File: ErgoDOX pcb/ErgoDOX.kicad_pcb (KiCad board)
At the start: 2 copper layers, 182.8 x 158.9 mm, 77 parts, among them J1 USB, J2 3.5mm, J3 JMP, J4 JMP, SW0:10 SW0:3, SW0:11 SW0:2, SW0:12 SW0:1, SW0:7 SW0:6, SW0:8 SW0:5, SW0:9 SW0:4, SW1:10 SW1:3, SW1:11 SW1:2, SW1:12 SW1:1, SW1:13 SW1:0, SW1:9 SW1:4, SW2:10 SW2:3, SW2:11 SW2:2, SW2:12 SW2:1, SW2:13 SW2:0, SW2:7 SW2:6, SW2:8 SW2:5, SW2:9 SW2:4, SW3:10 SW3:3, SW3:11 SW3:2, SW3:12 SW3:1, SW3:13 SW3:0, SW3:8 SW3:5, SW3:9 SW3:4, SW4:10 SW4:3, SW4:11 SW4:2, SW4:12 SW4:1, SW4:13 SW4:0, SW4:7 SW4:6, SW4:8 SW4:5, SW4:9 SW4:4, SW5:10 SW5:3, SW5:11 SW5:2, SW5:12 SW5:1, SW5:13 SW5:0, SW5:7 SW5:6, SW5:8 SW5:5, SW5:9 SW5:4, U1 TEENSY2.0, U2 MCP23018

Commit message: //WIP
Switches replaced
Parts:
- removed STAR_1: STAR_FRONT, ErgoDOX pcb:STAR
- removed STAR_2: STAR_BACK, ErgoDOX pcb:STAR
- removed STITCHING_VIA (x11): ~, lib_footprints:STITCHING_VIA
- added D1: DIODE, Diode_THT:D_DO-35_SOD27_P7.62mm_Horizontal, F.Cu at (68.6, 73.7)
- added D10: DIODE, Diode_THT:D_DO-35_SOD27_P7.62mm_Horizontal, F.Cu at (87.6, 111.8)
- added D11: DIODE, Diode_THT:D_DO-35_SOD27_P7.62mm_Horizontal, F.Cu at (106.7, 91.4)
- added D12: DIODE, Diode_THT:D_DO-35_SOD27_P7.62mm_Horizontal, F.Cu at (106.7, 110.5)
- added D13: DIODE, Diode_THT:D_DO-35_SOD27_P7.62mm_Horizontal, F.Cu at (125.7, 90.2)
- added D15: DIODE, Diode_THT:D_DO-35_SOD27_P7.62mm_Horizontal, F.Cu at (152.4, 91.4)
- added D16: DIODE, Diode_THT:D_DO-35_SOD27_P7.62mm_Horizontal, F.Cu at (152.4, 110.5)
- added D17: DIODE, Diode_THT:D_DO-35_SOD27_P7.62mm_Horizontal, F.Cu at (163.8, 95.2)
- added D18: DIODE, Diode_THT:D_DO-35_SOD27_P7.62mm_Horizontal, F.Cu at (163.8, 114.3)
- added D19: DIODE, Diode_THT:D_DO-35_SOD27_P7.62mm_Horizontal, F.Cu at (188.0, 95.2)
- added D2: DIODE, Diode_THT:D_DO-35_SOD27_P7.62mm_Horizontal, F.Cu at (87.6, 73.7)
- added D20: DIODE, Diode_THT:D_DO-35_SOD27_P7.62mm_Horizontal, F.Cu at (188.0, 114.3)
- added D21: DIODE, Diode_THT:D_DO-35_SOD27_P7.62mm_Horizontal, F.Cu at (81.3, 120.7)
- added D22: DIODE, Diode_THT:D_DO-35_SOD27_P7.62mm_Horizontal, F.Cu at (87.6, 130.8)
- added D23: DIODE, Diode_THT:D_DO-35_SOD27_P7.62mm_Horizontal, F.Cu at (106.7, 129.5)
- added D24: DIODE, Diode_THT:D_DO-35_SOD27_P7.62mm_Horizontal, F.Cu at (125.7, 128.3)
- added D25: DIODE, Diode_THT:D_DO-35_SOD27_P7.62mm_Horizontal, F.Cu at (152.4, 129.5)
- added D26: DIODE, Diode_THT:D_DO-35_SOD27_P7.62mm_Horizontal, F.Cu at (163.8, 133.3)
- added D27: DIODE, Diode_THT:D_DO-35_SOD27_P7.62mm_Horizontal, F.Cu at (188.0, 133.3)
- added D3: DIODE, Diode_THT:D_DO-35_SOD27_P7.62mm_Horizontal, F.Cu at (106.7, 72.4)
- added D4: DIODE, Diode_THT:D_DO-35_SOD27_P7.62mm_Horizontal, F.Cu at (125.7, 71.1)
- added D5: DIODE, Diode_THT:D_DO-35_SOD27_P7.62mm_Horizontal, F.Cu at (144.8, 72.4)
- added D6: DIODE, Diode_THT:D_DO-35_SOD27_P7.62mm_Horizontal, F.Cu at (163.8, 76.2)
- added D7: DIODE, Diode_THT:D_DO-35_SOD27_P7.62mm_Horizontal, F.Cu at (188.0, 76.2)
- added D8: DIODE, Diode_THT:D_DO-35_SOD27_P7.62mm_Horizontal, F.Cu at (81.3, 92.7)
- added D9: DIODE, Diode_THT:D_DO-35_SOD27_P7.62mm_Horizontal, F.Cu at (87.6, 92.7)
- SW0:10, SW0:11, SW0:12, SW0:7, SW0:8, SW0:9, SW1:10, SW1:11, SW1:12, SW1:13, SW1:9, SW2:10, SW2:11, SW2:12, SW2:7, SW2:8, SW2:9, SW3:10, SW3:11, SW3:12, SW3:8, SW3:9, SW4:10, SW4:11, SW4:12, SW4:7, SW4:8, SW4:9, SW5:10, SW5:11, SW5:12, SW5:7, SW5:8, SW5:9: footprint ErgoDOX pcb:MX_FLIP_DIODE -> Keyswitches Pretty:SW_PG1350_reversible
- SW2:13, SW3:13, SW4:13, SW5:13: footprint ErgoDOX pcb:MX_FLIP_XX -> Keyswitches Pretty:SW_PG1350_reversible
- SX0:10, SX0:11, SX1:7, SX1:8: footprint MX_FLIP -> Keyswitches Pretty:SW_PG1350_reversible
- moved LED_B1 10.2 mm to (62.2, 88.9)
- moved LED_C1 10.2 mm to (62.2, 117.5)
- moved LED_A1 9.22 mm to (72.4, 55.9)
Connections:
- SW0:10 pad 2: Net-(SW0:10-Pad2) -> Net-(D1:4-Pad1)
- SW0:11 pad 2: Net-(SW0:11-Pad2) -> Net-(D1:5-Pad1)
- SW0:12 pad 2: Net-(SW0:12-Pad2) -> Net-(D1:6-Pad1)
- SW0:7 pad 2: Net-(SW0:7-Pad2) -> Net-(D1:1-Pad1)
- SW0:8 pad 2: Net-(SW0:8-Pad2) -> Net-(D1:2-Pad1)
- SW0:9 pad 2: Net-(SW0:9-Pad2) -> Net-(D1:3-Pad1)
- SW2:10 pad 2: Net-(SW2:10-Pad2) -> Net-(D24-Pad1)
- SW2:11 pad 2: Net-(SW2:11-Pad2) -> Net-(D25-Pad1)
- SW2:12 pad 2: Net-(SW2:12-Pad2) -> Net-(D26-Pad1)
- SW2:13 pad 2: Net-(SW2:13-Pad2) -> Net-(D27-Pad1)
- SW2:7 pad 2: Net-(SW2:7-Pad2) -> Net-(D21-Pad1)
- SW2:8 pad 2: Net-(SW2:8-Pad2) -> Net-(D22-Pad1)
- SW2:9 pad 2: Net-(SW2:9-Pad2) -> Net-(D23-Pad1)
- SW3:10 pad 2: Net-(SW3:10-Pad2) -> Net-(D14-Pad1)
- SW3:11 pad 2: Net-(SW3:11-Pad2) -> Net-(D16-Pad1)
- SW3:12 pad 2: Net-(SW3:12-Pad2) -> Net-(D18-Pad1)
- SW3:13 pad 2: Net-(SW3:13-Pad2) -> Net-(D20-Pad1)
- SW3:8 pad 2: Net-(SW3:8-Pad2) -> Net-(D10-Pad1)
- SW3:9 pad 2: Net-(SW3:9-Pad2) -> Net-(D12-Pad1)
- SW4:10 pad 2: Net-(SW4:10-Pad2) -> Net-(D13-Pad1)
- SW4:11 pad 2: Net-(SW4:11-Pad2) -> Net-(D15-Pad1)
- SW4:12 pad 2: Net-(SW4:12-Pad2) -> Net-(D17-Pad1)
- SW4:13 pad 2: Net-(SW4:13-Pad2) -> Net-(D19-Pad1)
- SW4:7 pad 2: Net-(SW4:7-Pad2) -> Net-(D8-Pad1)
- SW4:8 pad 2: Net-(SW4:8-Pad2) -> Net-(D9-Pad1)
- SW4:9 pad 2: Net-(SW4:9-Pad2) -> Net-(D11-Pad1)
- SW5:10 pad 2: Net-(SW5:10-Pad2) -> Net-(D4-Pad1)
- SW5:11 pad 2: Net-(SW5:11-Pad2) -> Net-(D5-Pad1)
- SW5:12 pad 2: Net-(SW5:12-Pad2) -> Net-(D6-Pad1)
- SW5:13 pad 2: Net-(SW5:13-Pad2) -> Net-(D7-Pad1)
- SW5:7 pad 2: Net-(SW5:7-Pad2) -> Net-(D1-Pad1)
- SW5:8 pad 2: Net-(SW5:8-Pad2) -> Net-(D2-Pad1)
- SW5:9 pad 2: Net-(SW5:9-Pad2) -> Net-(D3-Pad1)
- SX0:10 pad 2: Net-(SW0:10-Pad2) -> Net-(D1:4-Pad1)
- SX0:11 pad 2: Net-(SW0:11-Pad2) -> Net-(D1:5-Pad1)
- U1 pad 12: Net-(U1-Pad12) -> (no net)
- U1 pad 19: Net-(U1-Pad19) -> (no net)
- U2 pad 14: Net-(U2-Pad14) -> (no net)
- U2 pad 17: Net-(U2-Pad17) -> (no net)
- U2 pad 18: Net-(U2-Pad18) -> (no net)
- U2 pad 19: Net-(U2-Pad19) -> (no net)
- U2 pad 27: Net-(U2-Pad27) -> (no net)
- U2 pad 28: Net-(U2-Pad28) -> (no net)
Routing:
- net /COL11: track 316.5 -> 256.5 mm
- net Net-(D20-Pad1): track 0.00 -> 45.5 mm
- net Net-(D19-Pad1): track 0.00 -> 45.4 mm
- net Net-(D7-Pad1): track 0.00 -> 45.4 mm
- net Net-(D27-Pad1): track 0.00 -> 45.0 mm
- net /ROW4: track 257.4 -> 215.6 mm
- net Net-(SW3:13-Pad2): track 38.1 -> 0.00 mm
- net Net-(SW4:13-Pad2): track 38.1 -> 0.00 mm
- net Net-(SW5:13-Pad2): track 38.0 -> 0.00 mm
- net Net-(SW2:13-Pad2): track 37.7 -> 0.00 mm
- net Net-(D1:4-Pad1): track 0.00 -> 29.2 mm
- net Net-(SW0:10-Pad2): track 34.8 -> 5.60 mm
- net Net-(D1:5-Pad1): track 0.00 -> 29.2 mm
- net Net-(SW0:11-Pad2): track 34.8 -> 5.61 mm
- net /COL1: track 291.8 -> 268.0 mm
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
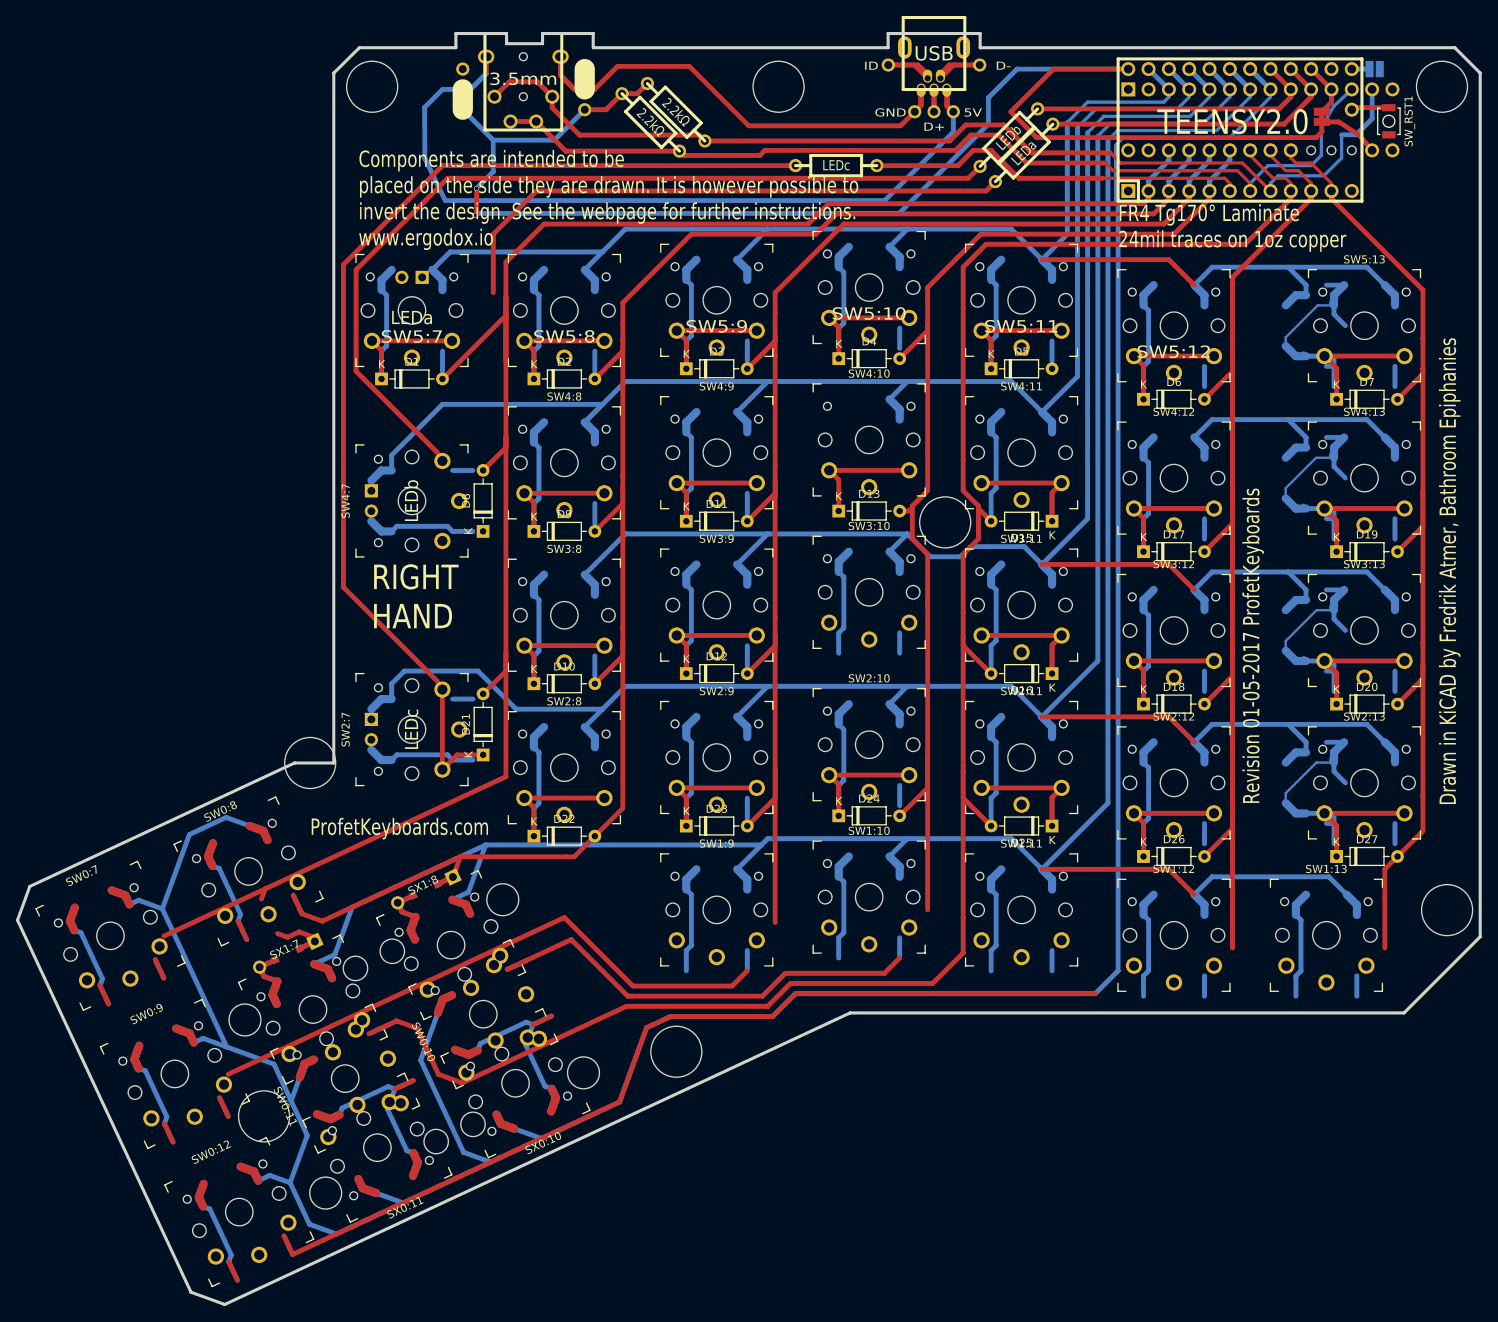
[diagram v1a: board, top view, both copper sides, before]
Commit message: WIP placement.py script, some routing
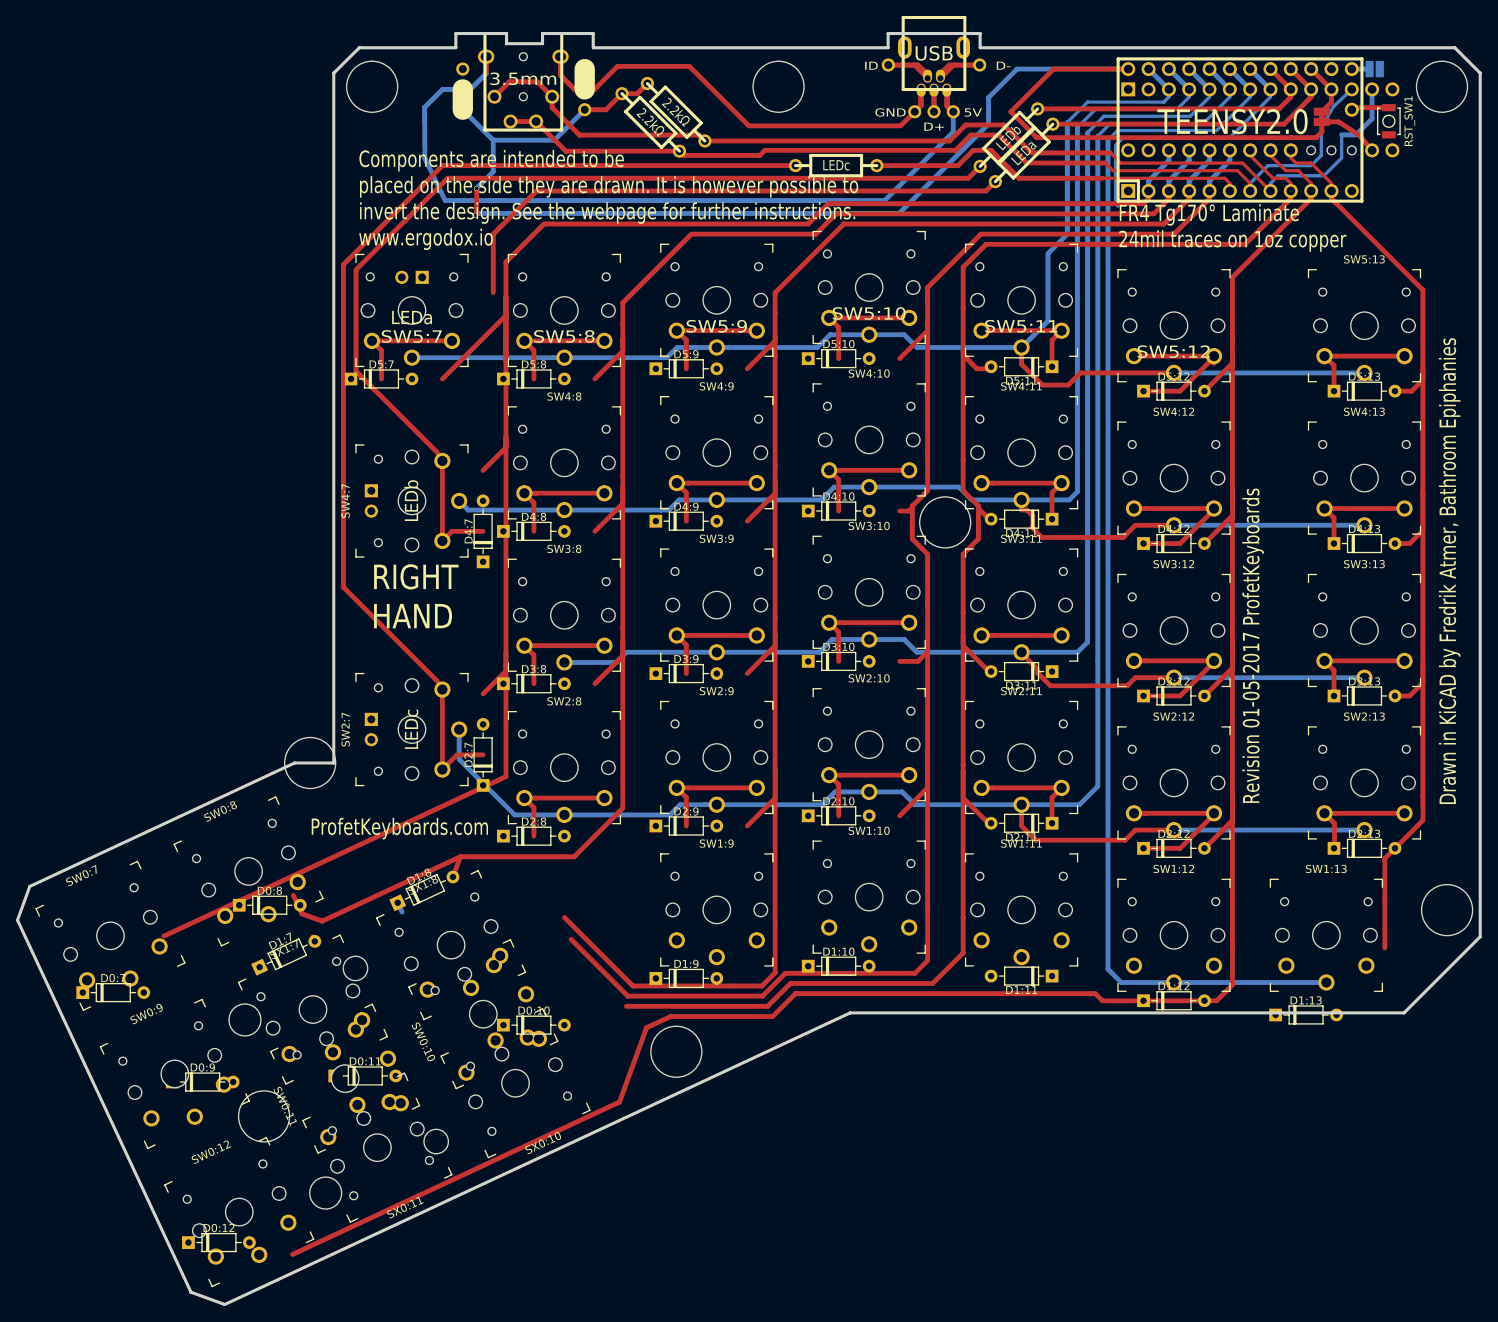
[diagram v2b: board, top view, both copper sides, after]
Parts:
- removed D17, D25, D26, D27, D6, D7: DIODE, Diode_THT:D_DO-35_SOD27_P7.62mm_Horizontal
- removed S2: STAB200, STAB_PCB940
- added D0:10: D0:3, ErgoDOX pcb:D_DO-35_SOD27_P7.62mm_Horizontal, F.Cu at (87.6, 154.4)
- added D0:11: D0:2, ErgoDOX pcb:D_DO-35_SOD27_P7.62mm_Horizontal, F.Cu at (66.5, 160.8)
- added D0:12: D0:1, ErgoDOX pcb:D_DO-35_SOD27_P7.62mm_Horizontal, F.Cu at (48.3, 181.6)
- added D0:7: D0:6, ErgoDOX pcb:D_DO-35_SOD27_P7.62mm_Horizontal, F.Cu at (35.1, 150.4)
- added D0:8: D0:5, ErgoDOX pcb:D_DO-35_SOD27_P7.62mm_Horizontal, F.Cu at (54.6, 139.4)
- added D0:9: D0:4, ErgoDOX pcb:D_DO-35_SOD27_P7.62mm_Horizontal, F.Cu at (46.2, 161.5)
- added D1:10: D1:3, ErgoDOX pcb:D_DO-35_SOD27_P7.62mm_Horizontal, F.Cu at (125.7, 147.1)
- added D1:11: D1:2, ErgoDOX pcb:D_DO-35_SOD27_P7.62mm_Horizontal, F.Cu at (148.6, 148.3)
- added D1:12: D1:1, ErgoDOX pcb:D_DO-35_SOD27_P7.62mm_Horizontal, F.Cu at (167.6, 151.4)
- added D1:13: D1:0, ErgoDOX pcb:D_DO-35_SOD27_P7.62mm_Horizontal, F.Cu at (184.2, 153.2)
- added D1:9: D1:4, ErgoDOX pcb:D_DO-35_SOD27_P7.62mm_Horizontal, F.Cu at (106.7, 148.6)
- added D2:11: D2:2, ErgoDOX pcb:D_DO-35_SOD27_P7.62mm_Horizontal, F.Cu at (148.6, 129.2)
- added D2:12: D2:1, ErgoDOX pcb:D_DO-35_SOD27_P7.62mm_Horizontal, F.Cu at (167.6, 132.3)
- added D2:13: D2:0, ErgoDOX pcb:D_DO-35_SOD27_P7.62mm_Horizontal, F.Cu at (191.5, 132.3)
- added D3:10: D3:3, ErgoDOX pcb:D_DO-35_SOD27_P7.62mm_Horizontal, F.Cu at (125.7, 109.0)
- added D4:12: D4:1, ErgoDOX pcb:D_DO-35_SOD27_P7.62mm_Horizontal, F.Cu at (167.6, 94.2)
- added D5:12: D5:1, ErgoDOX pcb:D_DO-35_SOD27_P7.62mm_Horizontal, F.Cu at (167.6, 75.2)
- added D5:13: D5:0, ErgoDOX pcb:D_DO-35_SOD27_P7.62mm_Horizontal, F.Cu at (191.5, 75.2)
- D1:7: value D -> D1:6; footprint DIODE -> ErgoDOX pcb:D_DO-35_SOD27_P7.62mm_Horizontal
- D1:8: value D -> D1:5; footprint DIODE -> ErgoDOX pcb:D_DO-35_SOD27_P7.62mm_Horizontal
- D2:10: renamed from D24; value DIODE -> D2:3; footprint Diode_THT:D_DO-35_SOD27_P7.62mm_Horizontal -> ErgoDOX pcb:D_DO-35_SOD27_P7.62mm_Horizontal
- D2:7: renamed from D21; value DIODE -> D2:6; footprint Diode_THT:D_DO-35_SOD27_P7.62mm_Horizontal -> ErgoDOX pcb:D_DO-35_SOD27_P7.62mm_Horizontal
- D2:8: renamed from D22; value DIODE -> D2:5; footprint Diode_THT:D_DO-35_SOD27_P7.62mm_Horizontal -> ErgoDOX pcb:D_DO-35_SOD27_P7.62mm_Horizontal
- D2:9: renamed from D23; value DIODE -> D2:4; footprint Diode_THT:D_DO-35_SOD27_P7.62mm_Horizontal -> ErgoDOX pcb:D_DO-35_SOD27_P7.62mm_Horizontal
- D3:11: renamed from D16; value DIODE -> D3:2; footprint Diode_THT:D_DO-35_SOD27_P7.62mm_Horizontal -> ErgoDOX pcb:D_DO-35_SOD27_P7.62mm_Horizontal
- D3:12: renamed from D18; value DIODE -> D3:1; footprint Diode_THT:D_DO-35_SOD27_P7.62mm_Horizontal -> ErgoDOX pcb:D_DO-35_SOD27_P7.62mm_Horizontal
- D3:13: renamed from D20; value DIODE -> D3:0; footprint Diode_THT:D_DO-35_SOD27_P7.62mm_Horizontal -> ErgoDOX pcb:D_DO-35_SOD27_P7.62mm_Horizontal
- D3:8: renamed from D10; value DIODE -> D3:5; footprint Diode_THT:D_DO-35_SOD27_P7.62mm_Horizontal -> ErgoDOX pcb:D_DO-35_SOD27_P7.62mm_Horizontal
- D3:9: renamed from D12; value DIODE -> D3:4; footprint Diode_THT:D_DO-35_SOD27_P7.62mm_Horizontal -> ErgoDOX pcb:D_DO-35_SOD27_P7.62mm_Horizontal
- D4:10: renamed from D13; value DIODE -> D4:3; footprint Diode_THT:D_DO-35_SOD27_P7.62mm_Horizontal -> ErgoDOX pcb:D_DO-35_SOD27_P7.62mm_Horizontal
- D4:11: renamed from D15; value DIODE -> D4:2; footprint Diode_THT:D_DO-35_SOD27_P7.62mm_Horizontal -> ErgoDOX pcb:D_DO-35_SOD27_P7.62mm_Horizontal
- D4:13: renamed from D19; value DIODE -> D4:0; footprint Diode_THT:D_DO-35_SOD27_P7.62mm_Horizontal -> ErgoDOX pcb:D_DO-35_SOD27_P7.62mm_Horizontal
- D4:7: renamed from D8; value DIODE -> D4:6; footprint Diode_THT:D_DO-35_SOD27_P7.62mm_Horizontal -> ErgoDOX pcb:D_DO-35_SOD27_P7.62mm_Horizontal
- D4:8: renamed from D9; value DIODE -> D4:5; footprint Diode_THT:D_DO-35_SOD27_P7.62mm_Horizontal -> ErgoDOX pcb:D_DO-35_SOD27_P7.62mm_Horizontal
- D4:9: renamed from D11; value DIODE -> D4:4; footprint Diode_THT:D_DO-35_SOD27_P7.62mm_Horizontal -> ErgoDOX pcb:D_DO-35_SOD27_P7.62mm_Horizontal
- D5:10: renamed from D4; value DIODE -> D5:3; footprint Diode_THT:D_DO-35_SOD27_P7.62mm_Horizontal -> ErgoDOX pcb:D_DO-35_SOD27_P7.62mm_Horizontal
- D5:11: renamed from D5; value DIODE -> D5:2; footprint Diode_THT:D_DO-35_SOD27_P7.62mm_Horizontal -> ErgoDOX pcb:D_DO-35_SOD27_P7.62mm_Horizontal
- D5:7: renamed from D1; value DIODE -> D5:6; footprint Diode_THT:D_DO-35_SOD27_P7.62mm_Horizontal -> ErgoDOX pcb:D_DO-35_SOD27_P7.62mm_Horizontal
- D5:8: renamed from D2; value DIODE -> D5:5; footprint Diode_THT:D_DO-35_SOD27_P7.62mm_Horizontal -> ErgoDOX pcb:D_DO-35_SOD27_P7.62mm_Horizontal
- D5:9: renamed from D3; value DIODE -> D5:4; footprint Diode_THT:D_DO-35_SOD27_P7.62mm_Horizontal -> ErgoDOX pcb:D_DO-35_SOD27_P7.62mm_Horizontal
- moved D3:12 3.94 mm to (167.6, 113.3)
- moved D5:11 3.82 mm to (148.6, 72.1), turned to 180 degrees
- moved D3:11 3.82 mm to (148.6, 110.2)
- moved D4:11 3.82 mm to (148.6, 91.2)
- moved D4:13 3.64 mm to (191.5, 94.2)
- moved D3:13 3.64 mm to (191.5, 113.3)
- renumbered SW_RST1 to RST_SW1
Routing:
- net /ROW0: track 404.2 -> 34.2 mm
- net /ROW1: track 302.9 -> 156.2 mm
- net /COL4: track 260.3 -> 205.8 mm
- net /COL11: track 256.5 -> 207.3 mm
- net /ROW2: track 273.8 -> 240.4 mm
- net Net-(D3:13-Pad1): track 45.5 -> 14.9 mm
- net Net-(D4:13-Pad1): track 45.4 -> 14.9 mm
- net Net-(D5:13-Pad1): track 45.4 -> 14.9 mm
- net Net-(D2:13-Pad1): track 45.0 -> 14.9 mm
- net /ROW5: track 203.6 -> 173.8 mm
- net Net-(D0:10-Pad1): track 29.2 -> 0.00 mm
- net Net-(D0:11-Pad1): track 29.2 -> 0.00 mm
- net /ROW4: track 215.6 -> 192.8 mm
- net /ROW3: track 220.3 -> 198.5 mm
- net Net-(SW0:9-Pad2): track 19.4 -> 0.00 mm
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
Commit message: placement, routing
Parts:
- moved D0:10 9.39 mm to (81.3, 161.4)
- moved D0:11 8.99 mm to (64.0, 169.4)
- moved D0:9 8.08 mm to (42.7, 168.8)
- moved D0:12 5.16 mm to (50.8, 186.1)
- moved D0:8 4.86 mm to (52.0, 143.5)
- moved D2:10 3.86 mm to (129.5, 127.7)
- moved D4:10 3.86 mm to (129.5, 89.6)
- moved D5:10 3.86 mm to (129.5, 70.5)
- moved D4:7 3.84 mm to (80.8, 88.9)
- moved D1:10 3.82 mm to (129.5, 146.7)
- moved D3:10 3.82 mm to (129.5, 108.6)
- moved D3:8 3.82 mm to (91.4, 111.5)
- moved D2:8 3.82 mm to (91.4, 130.5)
- moved D4:8 3.82 mm to (91.4, 92.4)
- moved D1:9 3.82 mm to (110.5, 148.3)
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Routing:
- net /COL6: track 233.8 -> 209.5 mm
- net /COL1: track 270.1 -> 255.7 mm
- net /COL4: track 205.8 -> 193.2 mm
- net /COL5: track 213.9 -> 202.1 mm
- net /COL11: track 207.3 -> 196.2 mm
- net /COL10: track 202.7 -> 192.0 mm
- net Net-(D3:11-Pad1): track 10.0 -> 15.0 mm
- net Net-(LED_A1-Pad1): track 72.8 -> 68.4 mm
- net Net-(D4:7-Pad1): track 15.6 -> 11.7 mm
- net /COL0: track 130.3 -> 126.8 mm
- net /ROW3: track 198.5 -> 199.4 mm

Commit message: //WIP
routing
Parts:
- moved D0:11 14.0 mm to (71.6, 157.6), turned to 115 degrees
- moved D0:10 14.0 mm to (88.8, 149.6), turned to 115 degrees
- moved D1:9 11.7 mm to (118.8, 140.0), turned to 90 degrees
- moved D1:10 11.7 mm to (137.8, 138.4), turned to 90 degrees
- moved D1:12 11.7 mm to (175.9, 143.2), turned to 90 degrees
- moved D1:13 11.7 mm to (195.0, 143.2), turned to 90 degrees
- moved D0:12 3.59 mm to (54.3, 185.3), turned to 25 degrees
- moved D0:7 3.59 mm to (38.2, 150.8), turned to 25 degrees
- moved D0:8 3.59 mm to (55.5, 142.7), turned to 25 degrees
- moved D0:9 3.59 mm to (46.3, 168.1), turned to 25 degrees
- moved D2:7 0.14 mm to (80.7, 117.5)
- moved D4:7 0.08 mm to (80.7, 88.9)
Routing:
- net /ROW0: track 34.2 -> 315.5 mm, vias 0 -> 2
- net /ROW1: track 156.2 -> 216.9 mm
- net /COL6: track 209.5 -> 164.0 mm
- net Net-(D0:10-Pad1): track 0.00 -> 26.0 mm
- net Net-(D0:11-Pad1): track 0.00 -> 25.6 mm
- net Net-(D1:7-Pad1): track 0.00 -> 22.0 mm
- net Net-(D1:11-Pad1): track 0.00 -> 20.8 mm
- net Net-(D0:12-Pad1): track 0.00 -> 14.8 mm
- net Net-(D0:9-Pad1): track 0.00 -> 14.8 mm
- net Net-(D0:7-Pad1): track 0.00 -> 14.8 mm
- net Net-(D0:8-Pad1): track 0.00 -> 14.8 mm
- net /COL0: track 126.8 -> 112.4 mm
- net Net-(D1:13-Pad1): track 0.00 -> 13.3 mm
- net Net-(D1:12-Pad1): track 0.00 -> 13.3 mm
- net Net-(D1:10-Pad1): track 0.00 -> 13.3 mm
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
